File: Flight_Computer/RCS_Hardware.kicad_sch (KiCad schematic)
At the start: 88 parts, among them J1 SWD, J10 Motor, J2 TYPE-C-31-M-12, J3 I2C, J4 5V, J5 GND, J6 AMT102, J7 FC_RF, J8 AMT102, Q1 2N7002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

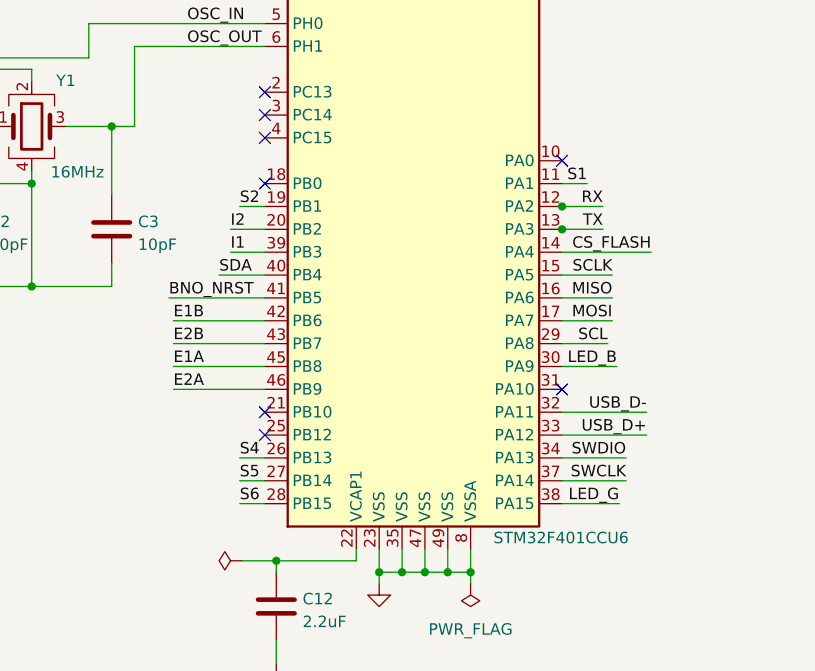
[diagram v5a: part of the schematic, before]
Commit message: updated gyro schematic and started placing PCB
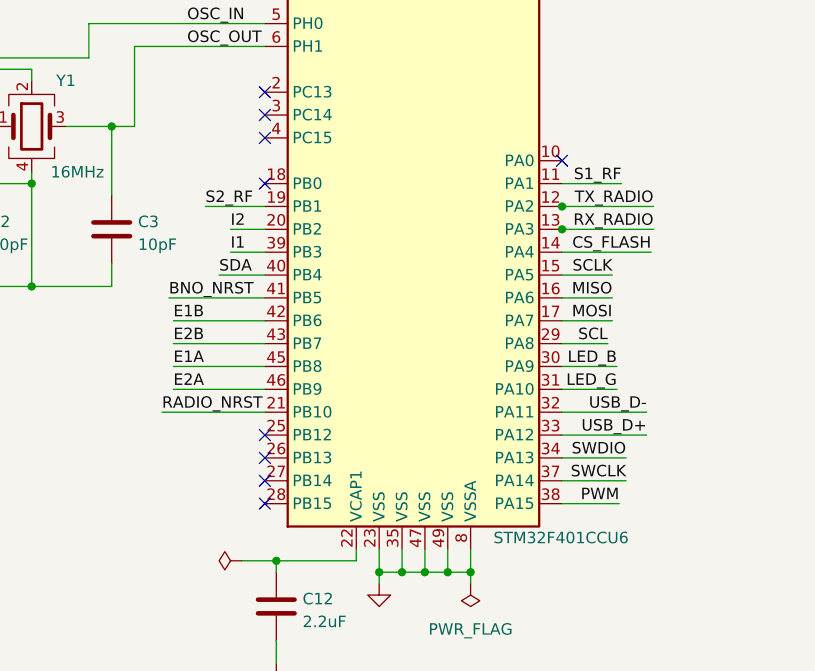
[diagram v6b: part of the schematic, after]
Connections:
- net RX is gone; now on net TX_RADIO: U1.12 (PA2)
- net S1 is gone; now on net S1_RF: U1.11 (PA1)
- net S2 is gone; now on net S2_RF: U1.19 (PB1)
- net TX is gone; now on net RX_RADIO: U1.13 (PA3)
- net LED_G: now also U1.31 (PA10); no longer U1.38 (PA15)
- net PWM: now also U1.38 (PA15)
- net RADIO_NRST: now also U1.21 (PB10)
- net S4: no longer names the net of U1.26 (PB13)
- net S5: no longer names the net of U1.27 (PB14)
- net S6: no longer names the net of U1.28 (PB15)
- no-connect marks 16 -> 17
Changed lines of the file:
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@@
 	)
 	(no_connect
-		(at 86.36 119.38)
-	)
-	(no_connect
 		(at 206.502 70.612)
 	)
@@
 	)
 	(no_connect
+		(at 86.36 124.46)
+	)
+	(no_connect
 		(at 242.062 68.072)
 	)
@@
 	)
 	(no_connect
-		(at 175.26 255.27)
+		(at 86.36 127)
 	)
 	(no_connect
-		(at 329.692 208.026)
+		(at 175.26 255.27)
 	)
 	(no_connect
-		(at 119.38 116.84)
+		(at 329.692 208.026)
 	)
 	(no_connect
@@
 		(at 234.188 210.058)
 	)
+	(no_connect
+		(at 86.36 129.54)
+	)
 	(wire
 		(pts
@@
 	(wire
 		(pts
+			(xy 119.38 116.84) (xy 125.476 116.84)
+		)
+		(stroke
+			(width 0)
+			(type default)
+		)
+	)
+	(wire
+		(pts
 			(xy 126.238 155.194) (xy 126.238 161.29)
 		)
@@
 	(wire
 		(pts
-			(xy 83.566 96.52) (xy 86.36 96.52)
+			(xy 79.756 96.52) (xy 86.36 96.52)
 		)
 		(stroke
@@
 	(wire
 		(pts
-			(xy 83.566 124.46) (xy 86.36 124.46)
-		)
-		(stroke
-			(width 0)
-			(type default)
-		)
-	)
-	(wire
-		(pts
 			(xy 107.95 34.29) (xy 107.95 35.56)
 		)
@@
 	(wire
 		(pts
-			(xy 71.882 87.63) (xy 69.342 87.63)
+			(xy 74.93 119.38) (xy 86.36 119.38)
 		)
 		(stroke
@@
 	(wire
 		(pts
-			(xy 62.992 36.83) (xy 62.992 39.37)
+			(xy 71.882 87.63) (xy 69.342 87.63)
 		)
 		(stroke
@@
 		)
 	)
-	(polyline
+	(wire
 		(pts
-			(xy 263.398 94.996) (xy 263.398 109.22)
+			(xy 62.992 36.83) (xy 62.992 39.37)
 		)
 		(stroke
@@
 		)
 	)
-	(wire
+	(polyline
 		(pts
-			(xy 83.566 129.54) (xy 86.36 129.54)
+			(xy 263.398 94.996) (xy 263.398 109.22)
 		)
 		(stroke
@@
 	(wire
 		(pts
-			(xy 123.9392 99.06) (xy 119.38 99.06)
+			(xy 129.54 99.06) (xy 119.38 99.06)
 		)
 		(stroke
@@
 	(wire
 		(pts
-			(xy 119.38 93.98) (xy 122.174 93.98)
+			(xy 119.38 93.98) (xy 125.984 93.98)
 		)
 		(stroke
@@
 	(wire
 		(pts
-			(xy 83.566 127) (xy 86.36 127)
-		)
-		(stroke
-			(width 0)
-			(type default)
-		)
-	)
-	(wire
-		(pts
-			(xy 123.9392 96.52) (xy 119.38 96.52)
+			(xy 129.54 96.52) (xy 119.38 96.52)
 		)
 		(stroke
@@
 		)
 	)
-	(label "LED_G"
+	(label "PWM"
 		(at 125.73 129.54 180)
 		(fields_autoplaced yes)
@@
 		)
 	)
-	(label "TX"
-		(at 123.9392 99.06 180)
+	(label "RX_RADIO"
+		(at 129.54 99.06 180)
 		(fields_autoplaced yes)
 		(effects
@@
 		)
 	)
-	(label "S6"
-		(at 83.566 129.54 0)
-		(fields_autoplaced yes)
-		(effects
-			(font
-				(size 1.27 1.27)
-			)
-			(justify left bottom)
-		)
-	)
 	(label "SCL"
 		(at 151.13 257.81 0)
@@
 		)
 	)
-	(label "S4"
-		(at 83.566 124.46 0)
-		(fields_autoplaced yes)
-		(effects
-			(font
-				(size 1.27 1.27)
-			)
-			(justify left bottom)
-		)
-	)
 	(label "I1"
 		(at 82.55 101.6 0)
@@
 		)
 	)
-	(label "S1"
-		(at 122.174 93.98 180)
+	(label "S1_RF"
+		(at 125.984 93.98 180)
 		(fields_autoplaced yes)
 		(effects
@@
 		)
 	)
-	(label "RX"
-		(at 123.9392 96.52 180)
+	(label "TX_RADIO"
+		(at 129.54 96.52 180)
 		(fields_autoplaced yes)
 		(effects
@@
 		)
 	)
-	(label "S2"
-		(at 83.566 96.52 0)
+	(label "S2_RF"
+		(at 79.756 96.52 0)
 		(fields_autoplaced yes)
 		(effects
@@
 		)
 	)
+	(label "LED_G"
+		(at 125.476 116.84 180)
+		(fields_autoplaced yes)
+		(effects
+			(font
+				(size 1.27 1.27)
+			)
+			(justify right bottom)
+		)
+	)
 	(label "PWM"
 		(at 262.89 200.66 0)
@@
 		)
 	)
-	(label "NRST"
-		(at 77.724 62.23 0)
+	(label "RADIO_NRST"
+		(at 74.93 119.38 0)
 		(fields_autoplaced yes)
 		(effects
@@
 		)
 	)
-	(label "SCL"
-		(at 325.628 215.646 0)
+	(label "NRST"
+		(at 77.724 62.23 0)
 		(fields_autoplaced yes)
 		(effects
@@
 		)
 	)
-	(label "S5"
-		(at 83.566 127 0)
+	(label "SCL"
+		(at 325.628 215.646 0)
 		(fields_autoplaced yes)
 		(effects

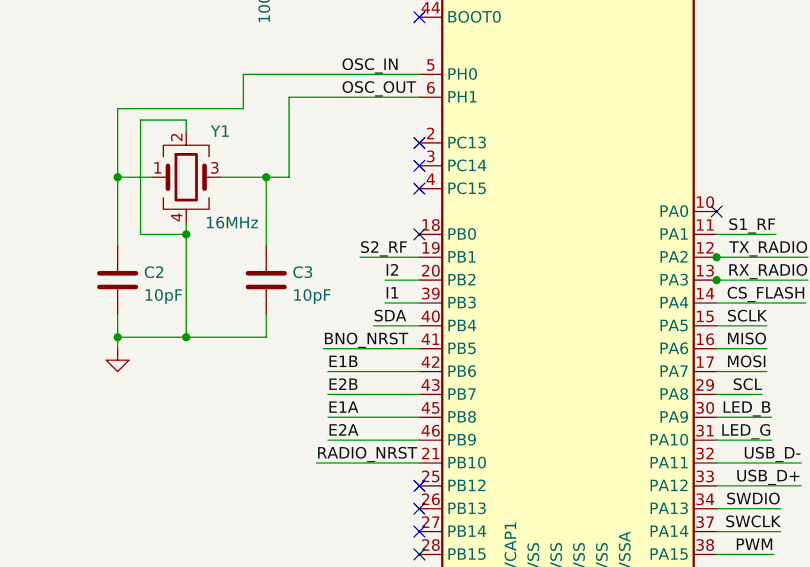
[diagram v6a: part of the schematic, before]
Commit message: finished (preliminary) placing of gyro pcb components
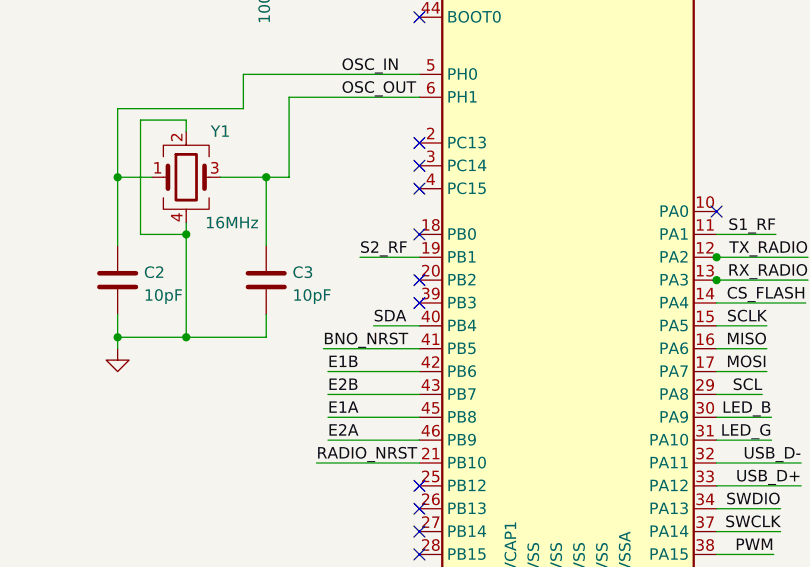
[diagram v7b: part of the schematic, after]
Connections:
- net I1: no longer names the net of U1.39 (PB3)
- net I2: no longer names the net of U1.20 (PB2)
- no-connect marks 17 -> 19
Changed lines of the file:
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@@
 	)
 	(no_connect
+		(at 86.36 99.06)
+	)
+	(no_connect
 		(at 234.188 207.518)
 	)
@@
 	)
 	(no_connect
+		(at 86.36 101.6)
+	)
+	(no_connect
 		(at 86.36 129.54)
 	)
@@
 	(wire
 		(pts
-			(xy 82.55 101.6) (xy 86.36 101.6)
-		)
-		(stroke
-			(width 0)
-			(type default)
-		)
-	)
-	(wire
-		(pts
 			(xy 200.406 189.992) (xy 200.406 191.008)
 		)
@@
 	(wire
 		(pts
-			(xy 82.55 99.06) (xy 86.36 99.06)
-		)
-		(stroke
-			(width 0)
-			(type default)
-		)
-	)
-	(wire
-		(pts
 			(xy 119.38 111.76) (xy 124.46 111.76)
 		)
@@
 		)
 	)
-	(label "I2"
-		(at 82.55 99.06 0)
-		(fields_autoplaced yes)
-		(effects
-			(font
-				(size 1.27 1.27)
-			)
-			(justify left bottom)
-		)
-	)
 	(label "USB_D-"
 		(at 195.072 68.072 180)
@@
 		)
 	)
-	(label "I1"
-		(at 82.55 101.6 0)
-		(fields_autoplaced yes)
-		(effects
-			(font
-				(size 1.27 1.27)
-			)
-			(justify left bottom)
-		)
-	)

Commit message: routed pcb
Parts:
- C27: value 150uF -> 100uF
- C28: value 680uF -> 470uF
- C3: JLCPCB# C32949 -> (none); LCSC Part (none) -> C1525
- L1: value 100uH -> 150uH
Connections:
- net VCC is gone; now on net +3.3V: J3.1 (Pin_1)
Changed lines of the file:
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@@
 		)
 	)
-	(label "VCC"
+	(label "+3.3V"
 		(at 128.778 197.358 180)
 		(fields_autoplaced yes)
@@
 			)
 		)
-		(property "Value" "680uF"
+		(property "Value" "470uF"
 			(at 222.504 162.56 0)
 			(effects
@@
 			)
 		)
-		(property "Value" "100uH"
+		(property "Value" "150uH"
 			(at 218.44 167.386 90)
 			(effects
@@
 			)
 		)
-		(property "Value" "150uF"
+		(property "Value" "100uF"
 			(at 167.894 165.862 0)
 			(effects
@@
 			)
 		)
-		(property "JLCPCB#" "C32949"
+		(property "LCSC Part" "C1525"
 			(at 69.342 99.06 0)
 			(effects
